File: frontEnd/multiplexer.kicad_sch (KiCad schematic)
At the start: 60 parts, among them J501 CH0_OUT, J502 CH0_IN, J503 CH1_OUT, J504 CH1_IN, J505 CH2_OUT, J506 CH2_IN, J507 CH3_OUT, J508 CH3_IN, J509 CH4_OUT, J510 CH4_IN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

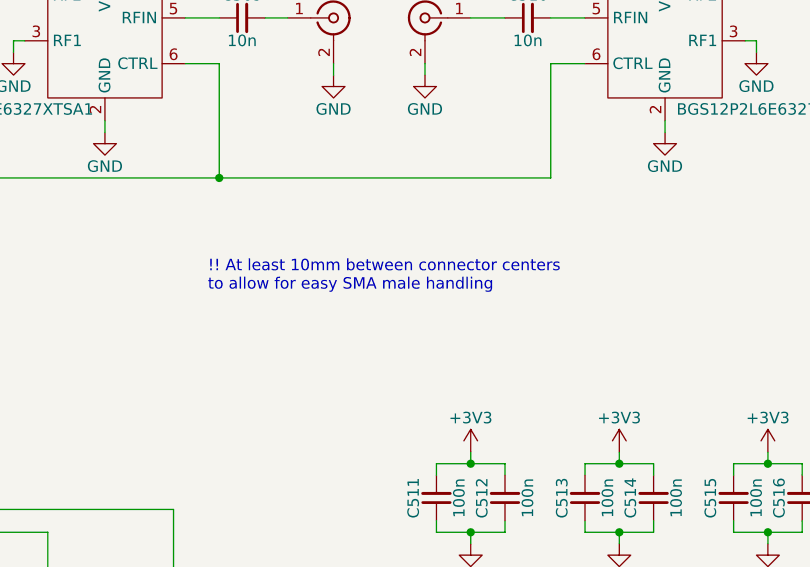
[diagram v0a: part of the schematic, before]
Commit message: add leds for each filter block
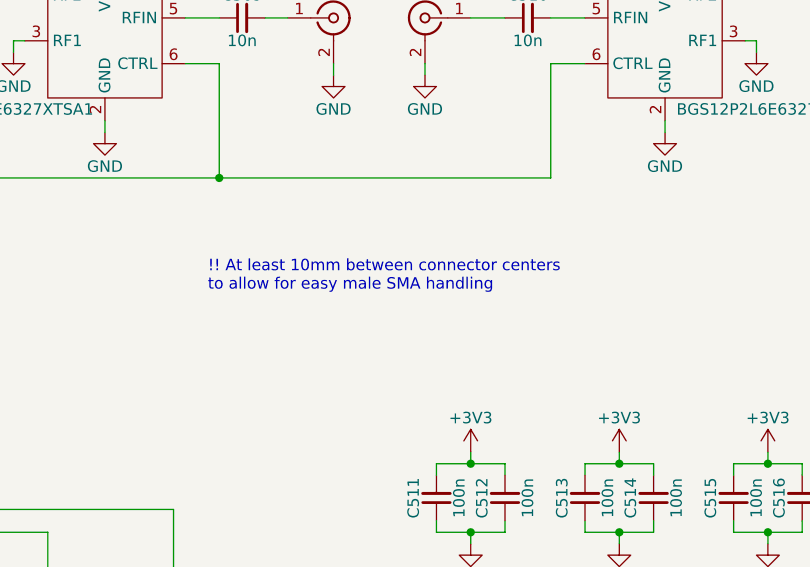
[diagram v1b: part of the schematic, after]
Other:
- note added: "!! At least 10mm between connector centers to allow for easy male SMA handling"
- note removed: "!! At least 10mm between connector centers to allow for easy SMA male handling"
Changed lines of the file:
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@@
     (stroke (width 0) (type default) (color 0 0 0 0))
   )
-  (text "!! At least 10mm between connector centers\nto allow for easy SMA male handling"
+  (text "!! At least 10mm between connector centers\nto allow for easy male SMA handling"
     (at 85.09 217.17 0)
     (effects (font (size 1.27 1.27)) (justify left bottom))

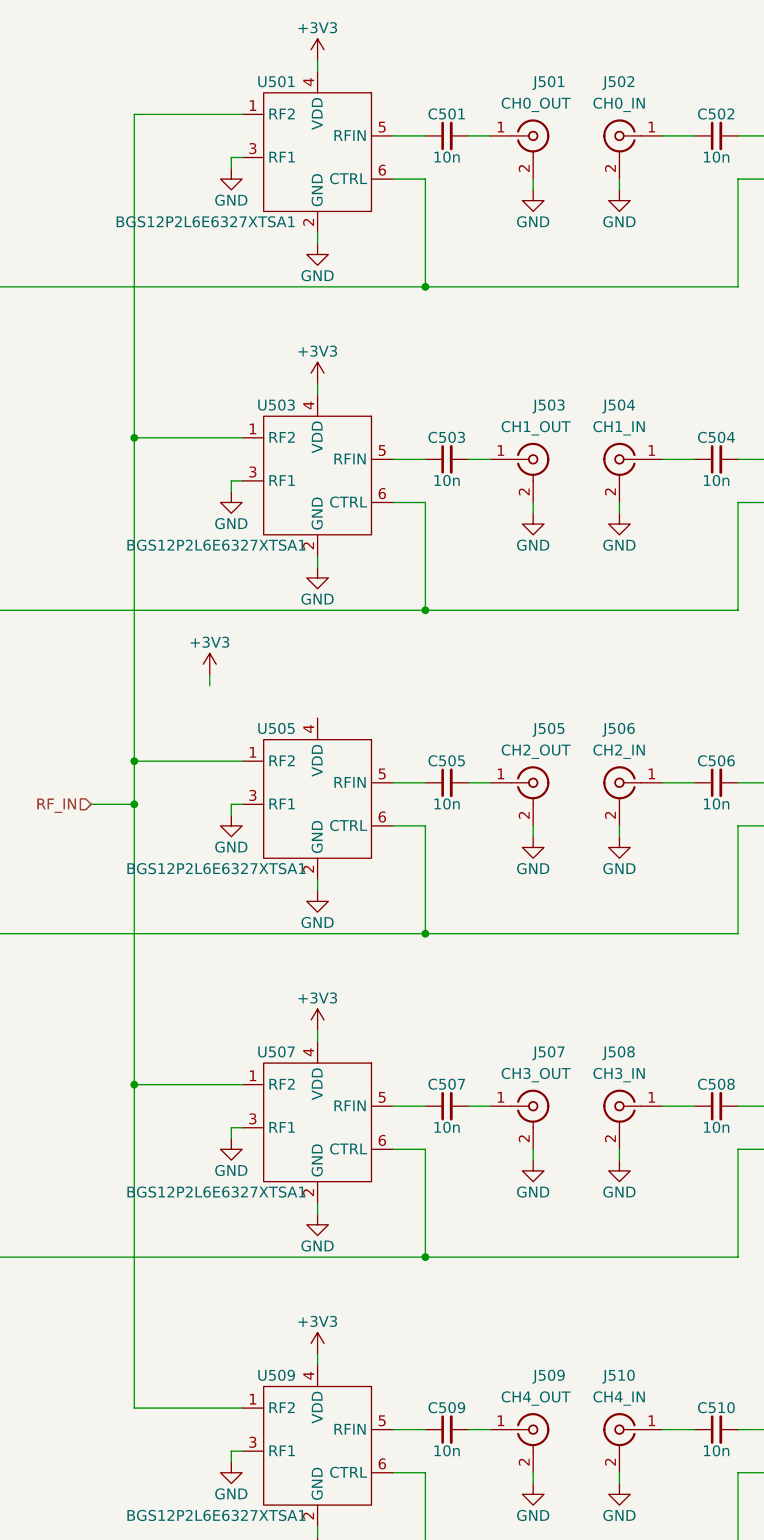
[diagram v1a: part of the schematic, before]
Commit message: assign footprints, part designators
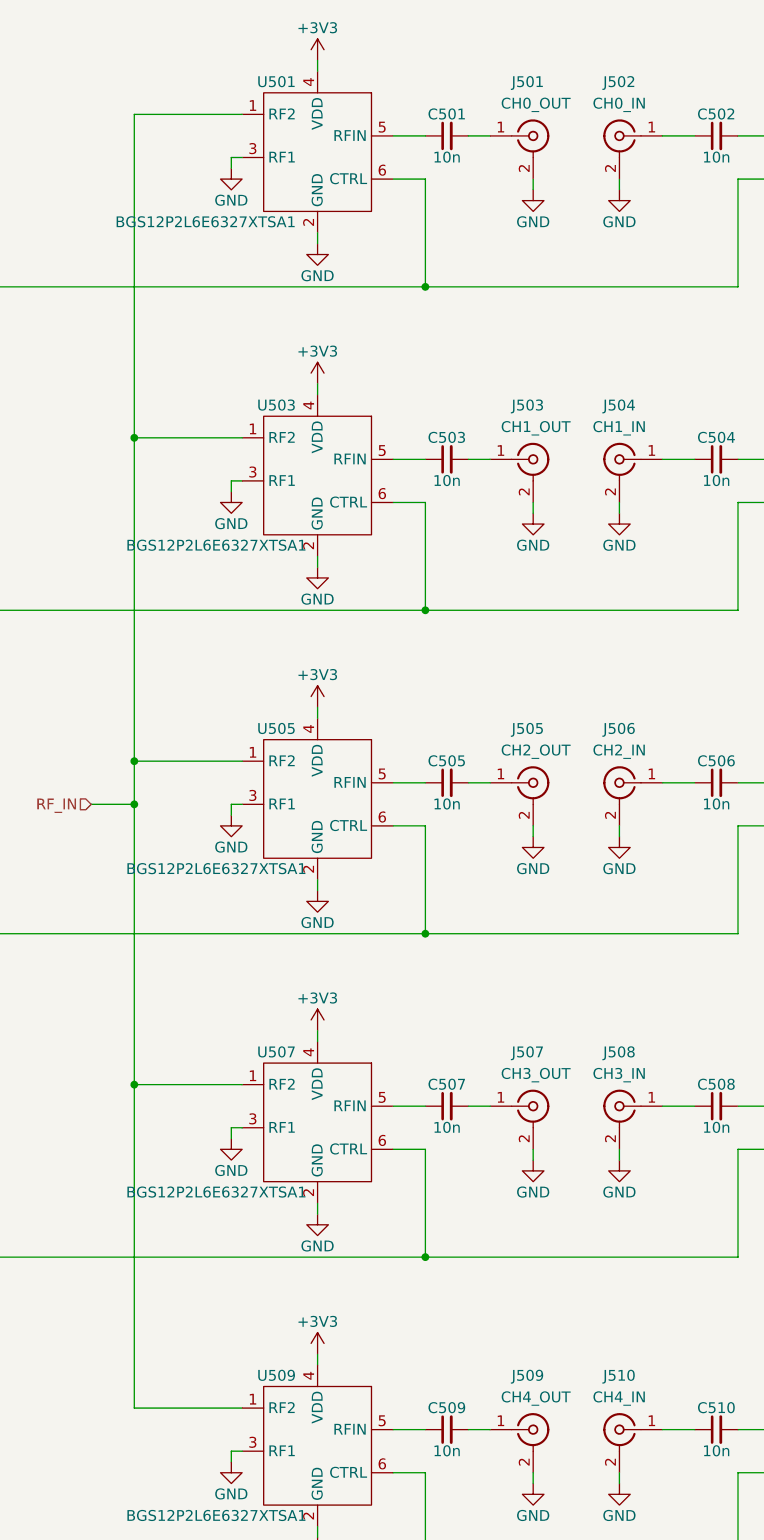
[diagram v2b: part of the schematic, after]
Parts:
- J501, J502, J503, J504, J505, J506, J507, J508, J509, J510: footprint (none) -> frontEnd:SMA_FEM_TH_VERTICAL
- U501, U502, U503, U504, U505, U506, U507, U508, U509, U510: footprint (none) -> frontEnd:BGS12P2L6E6327XTSA1
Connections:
- net +3V3: now also U505.4 (VDD)
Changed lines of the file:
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@@
     (stroke (width 0) (type default) (color 0 0 0 0))
   )
-  (wire (pts (xy 60.96 97.79) (xy 60.96 99.06))
+  (wire (pts (xy 73.66 101.6) (xy 73.66 102.87))
     (stroke (width 0) (type default) (color 0 0 0 0))
   )
@@
   (symbol (lib_id "Connector:Conn_Coaxial") (at 99.06 186.69 0) (unit 1)
     (in_bom yes) (on_board yes)
-    (property "Reference" "J509" (id 0) (at 99.06 180.34 0)
+    (property "Reference" "J509" (id 0) (at 96.52 180.34 0)
       (effects (font (size 1.27 1.27)) (justify left))
     )
@@
       (effects (font (size 1.27 1.27)) (justify left))
     )
-    (property "Footprint" "" (id 2) (at 99.06 186.69 0)
+    (property "Footprint" "frontEnd:SMA_FEM_TH_VERTICAL" (id 2) (at 99.06 186.69 0)
       (effects (font (size 1.27 1.27)) hide)
     )
@@
   (symbol (lib_id "Connector:Conn_Coaxial") (at 99.06 110.49 0) (unit 1)
     (in_bom yes) (on_board yes)
-    (property "Reference" "J505" (id 0) (at 99.06 104.14 0)
+    (property "Reference" "J505" (id 0) (at 96.52 104.14 0)
       (effects (font (size 1.27 1.27)) (justify left))
     )
@@
       (effects (font (size 1.27 1.27)) (justify left))
     )
-    (property "Footprint" "" (id 2) (at 99.06 110.49 0)
+    (property "Footprint" "frontEnd:SMA_FEM_TH_VERTICAL" (id 2) (at 99.06 110.49 0)
       (effects (font (size 1.27 1.27)) hide)
     )
@@
   (symbol (lib_id "Connector:Conn_Coaxial") (at 99.06 148.59 0) (unit 1)
     (in_bom yes) (on_board yes)
-    (property "Reference" "J507" (id 0) (at 99.06 142.24 0)
+    (property "Reference" "J507" (id 0) (at 96.52 142.24 0)
       (effects (font (size 1.27 1.27)) (justify left))
     )
@@
       (effects (font (size 1.27 1.27)) (justify left))
     )
-    (property "Footprint" "" (id 2) (at 99.06 148.59 0)
+    (property "Footprint" "frontEnd:SMA_FEM_TH_VERTICAL" (id 2) (at 99.06 148.59 0)
       (effects (font (size 1.27 1.27)) hide)
     )
@@
       (effects (font (size 1.27 1.27)) (justify left))
     )
-    (property "Footprint" "" (id 2) (at 80.01 72.39 0)
+    (property "Footprint" "frontEnd:BGS12P2L6E6327XTSA1" (id 2) (at 80.01 72.39 0)
       (effects (font (size 1.27 1.27)) hide)
     )
@@
   (symbol (lib_id "Connector:Conn_Coaxial") (at 99.06 72.39 0) (unit 1)
     (in_bom yes) (on_board yes)
-    (property "Reference" "J503" (id 0) (at 99.06 66.04 0)
+    (property "Reference" "J503" (id 0) (at 96.52 66.04 0)
       (effects (font (size 1.27 1.27)) (justify left))
     )
@@
       (effects (font (size 1.27 1.27)) (justify left))
     )
-    (property "Footprint" "" (id 2) (at 99.06 72.39 0)
+    (property "Footprint" "frontEnd:SMA_FEM_TH_VERTICAL" (id 2) (at 99.06 72.39 0)
       (effects (font (size 1.27 1.27)) hide)
     )
@@
       (effects (font (size 1.27 1.27)) (justify left))
     )
-    (property "Footprint" "" (id 2) (at 80.01 34.29 0)
+    (property "Footprint" "frontEnd:BGS12P2L6E6327XTSA1" (id 2) (at 80.01 34.29 0)
       (effects (font (size 1.27 1.27)) hide)
     )
@@
     (pin "2")
   )
-  (symbol (lib_id "power:+3V3") (at 60.96 97.79 0) (unit 1)
-    (in_bom yes) (on_board yes)
-    (property "Reference" "#PWR0513" (id 0) (at 60.96 101.6 0)
-      (effects (font (size 1.27 1.27)) hide)
-    )
-    (property "Value" "+3V3" (id 1) (at 60.96 93.98 0))
-    (property "Footprint" "" (id 2) (at 60.96 97.79 0)
-      (effects (font (size 1.27 1.27)) hide)
-    )
-    (property "Datasheet" "" (id 3) (at 60.96 97.79 0)
+  (symbol (lib_id "power:+3V3") (at 73.66 101.6 0) (unit 1)
+    (in_bom yes) (on_board yes)
+    (property "Reference" "#PWR0513" (id 0) (at 73.66 105.41 0)
+      (effects (font (size 1.27 1.27)) hide)
+    )
+    (property "Value" "+3V3" (id 1) (at 73.66 97.79 0))
+    (property "Footprint" "" (id 2) (at 73.66 101.6 0)
+      (effects (font (size 1.27 1.27)) hide)
+    )
+    (property "Datasheet" "" (id 3) (at 73.66 101.6 0)
       (effects (font (size 1.27 1.27)) hide)
     )
@@
       (effects (font (size 1.27 1.27)) (justify left))
     )
-    (property "Footprint" "" (id 2) (at 80.01 186.69 0)
+    (property "Footprint" "frontEnd:BGS12P2L6E6327XTSA1" (id 2) (at 80.01 186.69 0)
       (effects (font (size 1.27 1.27)) hide)
     )
@@
       (effects (font (size 1.27 1.27)) (justify left))
     )
-    (property "Footprint" "" (id 2) (at 80.01 110.49 0)
+    (property "Footprint" "frontEnd:BGS12P2L6E6327XTSA1" (id 2) (at 80.01 110.49 0)
       (effects (font (size 1.27 1.27)) hide)
     )
@@
       (effects (font (size 1.27 1.27)) (justify left))
     )
-    (property "Footprint" "" (id 2) (at 129.54 110.49 0)
+    (property "Footprint" "frontEnd:BGS12P2L6E6327XTSA1" (id 2) (at 129.54 110.49 0)
       (effects (font (size 1.27 1.27)) hide)
     )
@@
     (property "Reference" "J504" (id 0) (at 109.22 66.04 0))
     (property "Value" "CH1_IN" (id 1) (at 109.22 68.58 0))
-    (property "Footprint" "" (id 2) (at 109.22 72.39 0)
+    (property "Footprint" "frontEnd:SMA_FEM_TH_VERTICAL" (id 2) (at 109.22 72.39 0)
       (effects (font (size 1.27 1.27)) hide)
     )
@@
     (property "Reference" "J508" (id 0) (at 109.22 142.24 0))
     (property "Value" "CH3_IN" (id 1) (at 109.22 144.78 0))
-    (property "Footprint" "" (id 2) (at 109.22 148.59 0)
+    (property "Footprint" "frontEnd:SMA_FEM_TH_VERTICAL" (id 2) (at 109.22 148.59 0)
       (effects (font (size 1.27 1.27)) hide)
     )
@@
       (effects (font (size 1.27 1.27)) (justify left))
     )
-    (property "Footprint" "" (id 2) (at 80.01 148.59 0)
+    (property "Footprint" "frontEnd:BGS12P2L6E6327XTSA1" (id 2) (at 80.01 148.59 0)
       (effects (font (size 1.27 1.27)) hide)
     )
@@
       (effects (font (size 1.27 1.27)) (justify left))
     )
-    (property "Footprint" "" (id 2) (at 129.54 186.69 0)
+    (property "Footprint" "frontEnd:BGS12P2L6E6327XTSA1" (id 2) (at 129.54 186.69 0)
       (effects (font (size 1.27 1.27)) hide)
     )
@@
   (symbol (lib_id "Connector:Conn_Coaxial") (at 99.06 34.29 0) (unit 1)
     (in_bom yes) (on_board yes)
-    (property "Reference" "J501" (id 0) (at 99.06 27.94 0)
+    (property "Reference" "J501" (id 0) (at 96.52 27.94 0)
       (effects (font (size 1.27 1.27)) (justify left))
     )
@@
       (effects (font (size 1.27 1.27)) (justify left))
     )
-    (property "Footprint" "" (id 2) (at 99.06 34.29 0)
+    (property "Footprint" "frontEnd:SMA_FEM_TH_VERTICAL" (id 2) (at 99.06 34.29 0)
       (effects (font (size 1.27 1.27)) hide)
     )
@@
       (effects (font (size 1.27 1.27)) (justify left))
     )
-    (property "Footprint" "" (id 2) (at 129.54 148.59 0)
+    (property "Footprint" "frontEnd:BGS12P2L6E6327XTSA1" (id 2) (at 129.54 148.59 0)
       (effects (font (size 1.27 1.27)) hide)
     )
@@
     (property "Reference" "J510" (id 0) (at 109.22 180.34 0))
     (property "Value" "CH4_IN" (id 1) (at 109.22 182.88 0))
-    (property "Footprint" "" (id 2) (at 109.22 186.69 0)
+    (property "Footprint" "frontEnd:SMA_FEM_TH_VERTICAL" (id 2) (at 109.22 186.69 0)
       (effects (font (size 1.27 1.27)) hide)
     )
@@
       (effects (font (size 1.27 1.27)) (justify left))
     )
-    (property "Footprint" "" (id 2) (at 129.54 72.39 0)
+    (property "Footprint" "frontEnd:BGS12P2L6E6327XTSA1" (id 2) (at 129.54 72.39 0)
       (effects (font (size 1.27 1.27)) hide)
     )
@@
     (property "Reference" "J506" (id 0) (at 109.22 104.14 0))
     (property "Value" "CH2_IN" (id 1) (at 109.22 106.68 0))
-    (property "Footprint" "" (id 2) (at 109.22 110.49 0)
+    (property "Footprint" "frontEnd:SMA_FEM_TH_VERTICAL" (id 2) (at 109.22 110.49 0)
       (effects (font (size 1.27 1.27)) hide)
     )
@@
       (effects (font (size 1.27 1.27)) (justify left))
     )
-    (property "Footprint" "" (id 2) (at 129.54 34.29 0)
+    (property "Footprint" "frontEnd:BGS12P2L6E6327XTSA1" (id 2) (at 129.54 34.29 0)
       (effects (font (size 1.27 1.27)) hide)
     )
@@
     (property "Reference" "J502" (id 0) (at 109.22 27.94 0))
     (property "Value" "CH0_IN" (id 1) (at 109.22 30.48 0))
-    (property "Footprint" "" (id 2) (at 109.22 34.29 0)
-      (effects (font (size 1.27 1.27)) hide)
-    )
+    (property "Footprint" "frontEnd:SMA_FEM_TH_VERTICAL" (id 2) (at 109.22 34.29 0)
+      (effects (font (size 1.27 1.27)) hide)
+    )
